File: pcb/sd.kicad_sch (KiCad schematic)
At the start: 1 part, among them J4 Micro_SD_Card_Det1

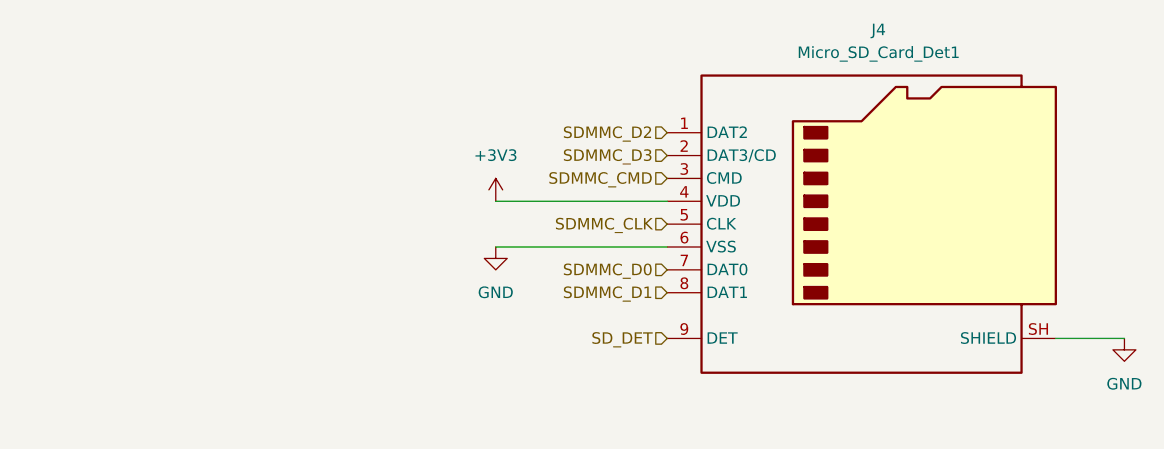
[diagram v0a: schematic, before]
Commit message: fix JOURNAL.md hour formatting
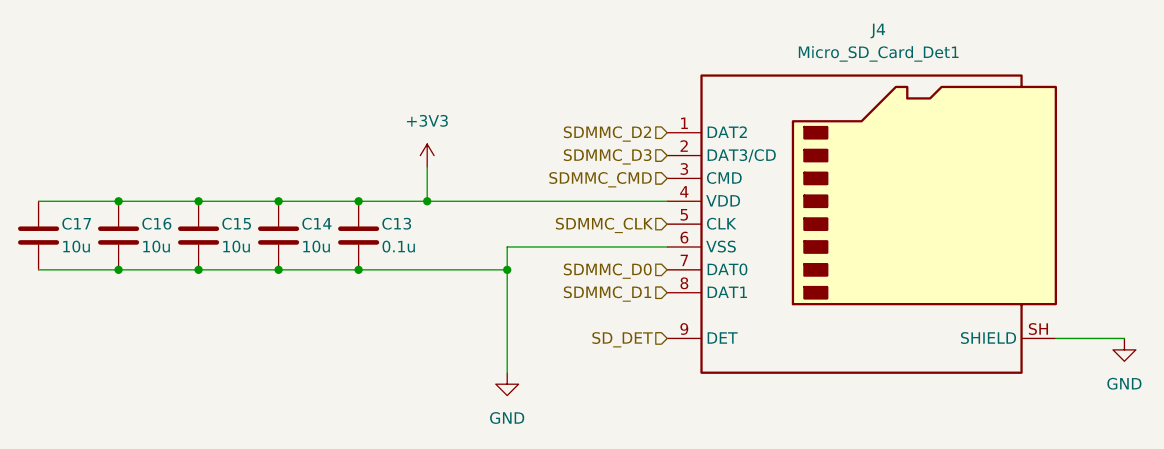
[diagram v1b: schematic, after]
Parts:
- added C13: 0.1u, symbol Device:C
- added C14, C15, C16, C17: 10u, symbol Device:C
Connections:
- net +3V3: now also C13.1, C14.1, C15.1, C16.1, C17.1
- net GND: now also C13.2, C14.2, C15.2, C16.2, C17.2

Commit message: layout pcb
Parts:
- C13, C14, C15, C16, C17: footprint (none) -> Capacitor_SMD:C_0805_2012Metric_Pad1.18x1.45mm_HandSolder
- J4: footprint (none) -> Connector_Card:microSD_HC_Hirose_DM3AT-SF-PEJM5
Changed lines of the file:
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@@
 			)
 		)
-		(property "Footprint" ""
+		(property "Footprint" "Capacitor_SMD:C_0805_2012Metric_Pad1.18x1.45mm_HandSolder"
 			(at 26.3652 73.66 0)
 			(hide yes)
@@
 			)
 		)
-		(property "Footprint" ""
+		(property "Footprint" "Capacitor_SMD:C_0805_2012Metric_Pad1.18x1.45mm_HandSolder"
 			(at 17.4752 73.66 0)
 			(hide yes)
@@
 			)
 		)
-		(property "Footprint" ""
+		(property "Footprint" "Capacitor_SMD:C_0805_2012Metric_Pad1.18x1.45mm_HandSolder"
 			(at 44.1452 73.66 0)
 			(hide yes)
@@
 			)
 		)
-		(property "Footprint" ""
+		(property "Footprint" "Connector_Card:microSD_HC_Hirose_DM3AT-SF-PEJM5"
 			(at 161.29 50.8 0)
 			(hide yes)
@@
 			)
 		)
-		(property "Footprint" ""
+		(property "Footprint" "Capacitor_SMD:C_0805_2012Metric_Pad1.18x1.45mm_HandSolder"
 			(at 35.2552 73.66 0)
 			(hide yes)
@@
 			)
 		)
-		(property "Footprint" ""
+		(property "Footprint" "Capacitor_SMD:C_0805_2012Metric_Pad1.18x1.45mm_HandSolder"
 			(at 53.0352 73.66 0)
 			(hide yes)
